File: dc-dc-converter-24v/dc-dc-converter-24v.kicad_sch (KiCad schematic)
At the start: 1 part, among them U1 LM5175PWPT

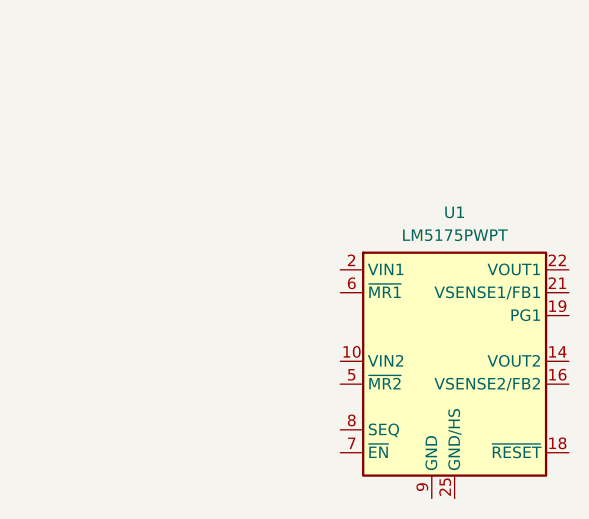
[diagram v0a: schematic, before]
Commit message: update symbol in DC-DC converter
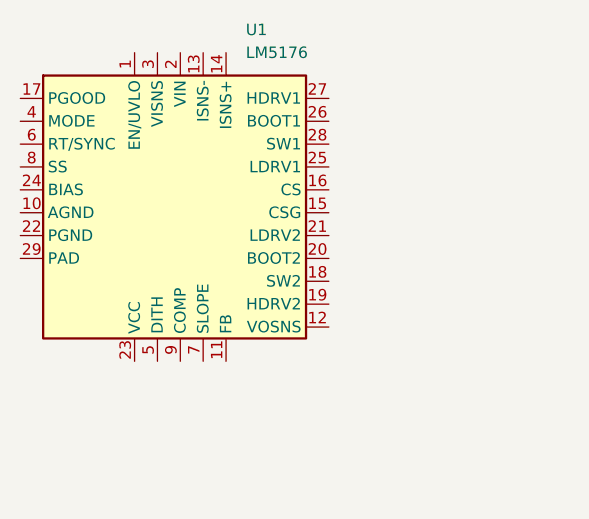
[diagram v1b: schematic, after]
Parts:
- removed U1: LM5175PWPT, benediktibk:LM5175PWPT, symbol benediktibk:LM5175PWPT
- added U1: LM5176, benediktibk:LM5176, symbol benediktibk:LM5176
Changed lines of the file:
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@@
 (kicad_sch (version 20230121) (generator eeschema)
   (paper "A4")
-  (symbol (lib_id "benediktibk:LM5175PWPT") (at 147.32 101.6 0) (unit 1)
+  (symbol (lib_id "benediktibk:LM5176") (at 111.76 82.55 0) (unit 1)
     (in_bom yes) (on_board yes) (dnp no) (fields_autoplaced)
-    (property "Reference" "U1" (at 147.32 85.09 0)
-      (effects (font (size 1.27 1.27)))
+    (property "Reference" "U1" (at 124.1141 64.77 0)
+      (effects (font (size 1.27 1.27)) (justify left))
     )
-    (property "Value" "LM5175PWPT" (at 147.32 87.63 0)
-      (effects (font (size 1.27 1.27)))
+    (property "Value" "LM5176" (at 124.1141 67.31 0)
+      (effects (font (size 1.27 1.27)) (justify left))
     )
-    (property "Footprint" "benediktibk:LM5175PWPT" (at 146.685 85.725 0)
+    (property "Footprint" "benediktibk:LM5176" (at 116.84 82.55 0)
       (effects (font (size 1.27 1.27) italic) hide)
     )
-    (property "Datasheet" "" (at 147.32 101.6 0)
+    (property "Datasheet" "" (at 111.76 82.55 0)
       (effects (font (size 1.27 1.27)) hide)
     )
-    (property "RS order number" "908-3877" (at 147.32 101.6 0)
+    (property "RS order number" "" (at 111.76 82.55 0)
       (effects (font (size 1.27 1.27)) hide)
     )
+    (pin "21")
+    (pin "7")
+    (pin "26")
+    (pin "24")
     (pin "22")
-    (pin "14")
-    (pin "2")
-    (pin "6")
-    (pin "3")
-    (pin "21")
-    (pin "17")
-    (pin "16")
-    (pin "7")
-    (pin "4")
-    (pin "9")
-    (pin "19")
-    (pin "5")
-    (pin "15")
-    (pin "23")
-    (pin "13")
-    (pin "24")
-    (pin "8")
-    (pin "1")
     (pin "11")
     (pin "10")
+    (pin "18")
+    (pin "25")
+    (pin "3")
+    (pin "6")
+    (pin "16")
+    (pin "28")
     (pin "20")
-    (pin "25")
+    (pin "2")
+    (pin "17")
+    (pin "19")
+    (pin "9")
+    (pin "1")
+    (pin "27")
+    (pin "23")
+    (pin "8")
+    (pin "5")
+    (pin "4")
+    (pin "13")
     (pin "12")
-    (pin "18")
+    (pin "14")
+    (pin "15")
+    (pin "29")
     (instances
       (project "dc-dc-converter-24v"

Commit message: work on DC DC converter
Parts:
- added C1: 470uF, symbol benediktibk:C_470uF_SMD_63V_20%
- added C2: C_240pF_SMD_0805_250V_10%, benediktibk:C_0805_2012Metric_Pad1.18x1.45mm_HandSolder, symbol benediktibk:C_240pF_SMD_0805_250V_10%
- added C3, C6: 47uF, benediktibk:C_1206_3216Metric_Pad1.33x1.80mm_HandSolder, symbol benediktibk:C_47uF_SMD_1206_25V_20%
- added C4, C5: 4.7uF, benediktibk:C_0805_2012Metric_Pad1.18x1.45mm_HandSolder, symbol benediktibk:C_4_7uF_SMD_0805_50V_10%
- added C7: 1uF, benediktibk:C_0603_1608Metric_Pad1.08x0.95mm_HandSolder, symbol benediktibk:C_1uF_SMD_0603_50V_10%
- added C8, C9: 100nF, benediktibk:C_0603_1608Metric_Pad1.08x0.95mm_HandSolder, symbol benediktibk:C_100nF_SMD_0603_50V
- added H1, H2, H3, H4: MountingHole_Pad_M6, benediktibk:MountingHole_6.4mm_M6_Pad_TopBottom, symbol benediktibk:MountingHole_Pad_M6
- added J1: 24V, benediktibk:Connector_M6, symbol benediktibk:Connector_M6
- added J2: 12V, benediktibk:Connector_M6, symbol benediktibk:Connector_M6
- added J3, J4: GND, benediktibk:Connector_M6, symbol benediktibk:Connector_M6
- added L1: L_2_5µH_30A, symbol benediktibk:L_2_5µH_30A
- added R1: 24kOhm, benediktibk:R_0603_1608Metric_Pad0.98x0.95mm_HandSolder, symbol benediktibk:R_24kOhm_SMD_0603_100mW_1%
- added R2: 4mOhm, benediktibk:R_2512_6332Metric_Pad1.40x3.35mm_HandSolder, symbol benediktibk:R_4mOhm_SMD_2512_2W_1%
- added R3: R_220kOhm_SMD_0603_100mW_1%, benediktibk:R_0603_1608Metric_Pad0.98x0.95mm_HandSolder, symbol benediktibk:R_220kOhm_SMD_0603_100mW_1%
- added R4: R_43kOhm_SMD_0603_100mW_1%, benediktibk:R_0603_1608Metric_Pad0.98x0.95mm_HandSolder, symbol benediktibk:R_43kOhm_SMD_0603_100mW_1%
- added R5: R_93_1kOhm_SMD_0603_100mW_1%, benediktibk:R_0603_1608Metric_Pad0.98x0.95mm_HandSolder, symbol benediktibk:R_93_1kOhm_SMD_0603_100mW_1%
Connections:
- net GND: now reaches U1.10 (AGND)
- net GND: now also U1.22 (PGND), U1.29 (PAD), C1.2, C2.2, C3.2, C4.2, C5.2, C6.2, C7.2, C8.2, C9.2, J3.1 (Pin_1), J4.1 (Pin_1), R1.2
- net Vout: now reaches U1.24 (BIAS)
- net Vout: now also C1.1, C3.1, C5.1, C8.1, J1.1 (Pin_1)
- net at U1.6 (RT/SYNC): now also R1.1
- net at U1.7 (SLOPE): now also C2.1
- net at U1.8 (SS): now also C9.1
- new net: C4.1, C6.1, C7.1, J2.1 (Pin_1)
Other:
- moved on the sheet: U1

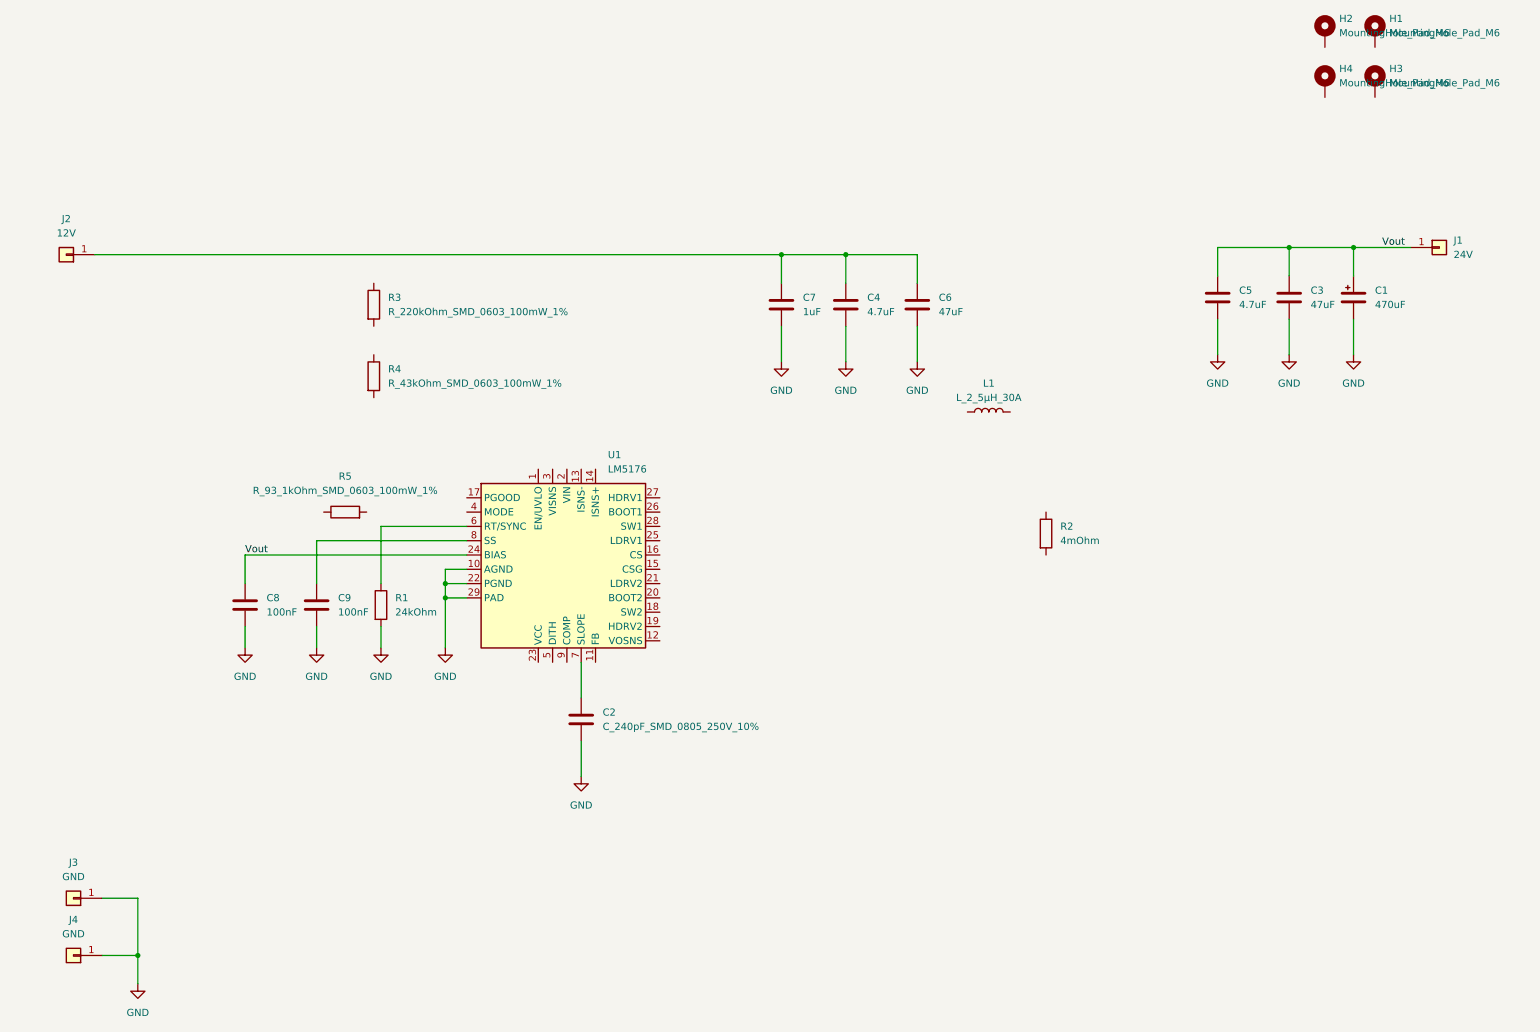
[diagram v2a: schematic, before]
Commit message: continue with design of DC-DC converter
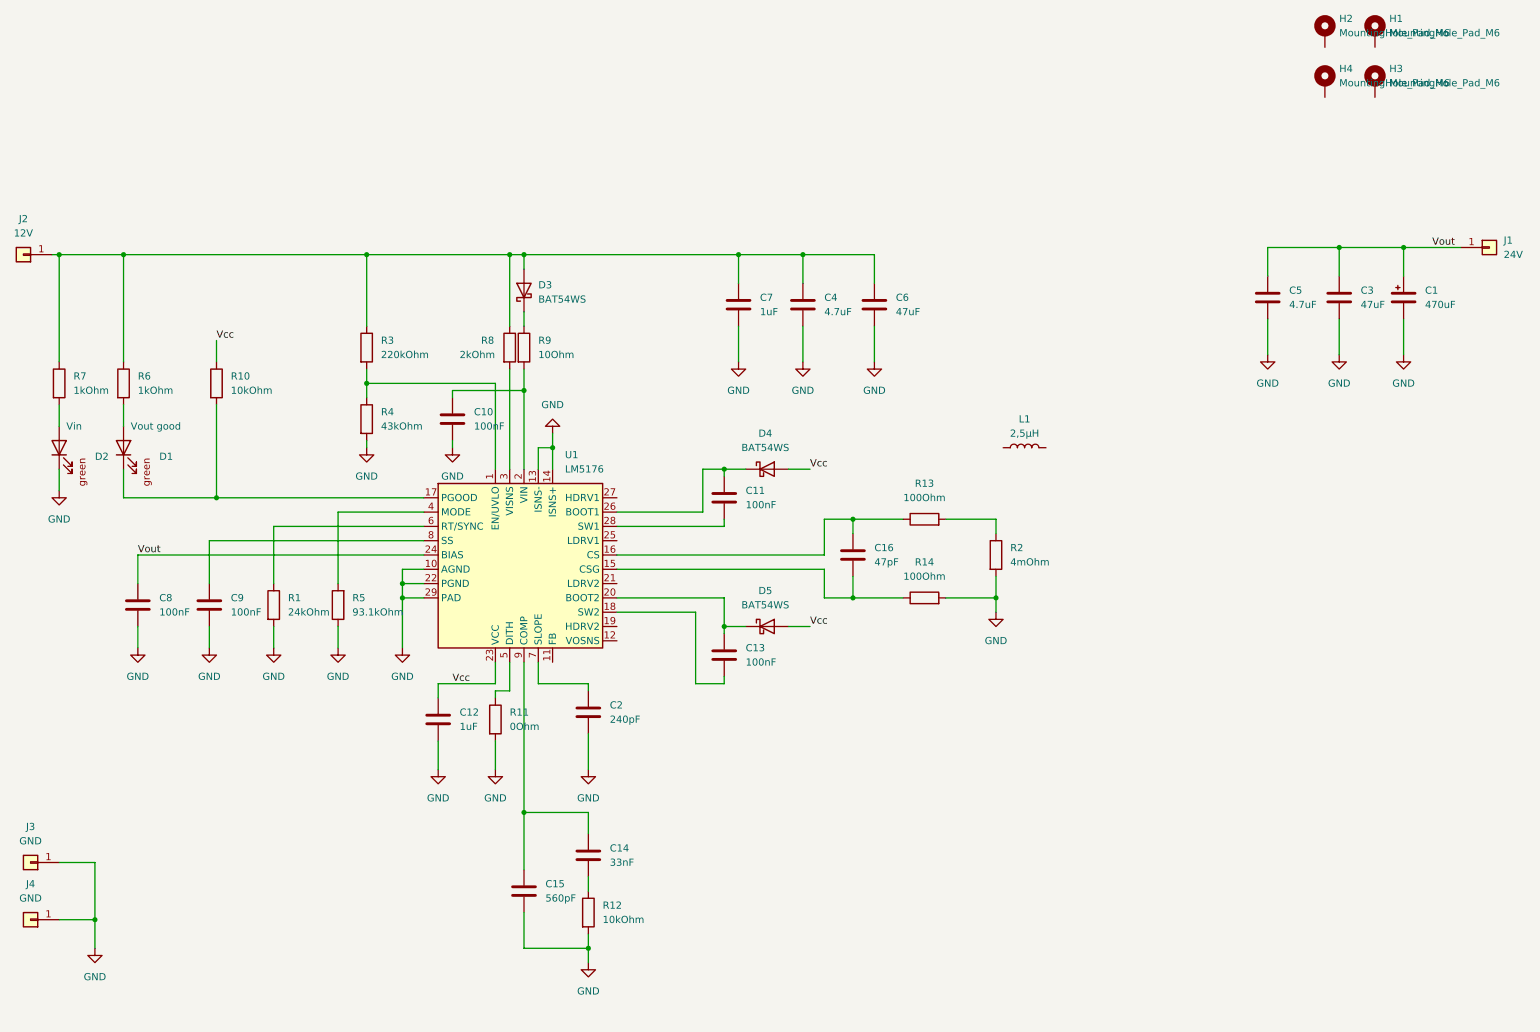
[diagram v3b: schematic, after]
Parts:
- added C10, C11, C13: 100nF, benediktibk:C_0603_1608Metric_Pad1.08x0.95mm_HandSolder, symbol benediktibk:C_100nF_SMD_0603_50V
- added C12: 1uF, benediktibk:C_0603_1608Metric_Pad1.08x0.95mm_HandSolder, symbol benediktibk:C_1uF_SMD_0603_50V_10%
- added C14: 33nF, benediktibk:C_0603_1608Metric_Pad1.08x0.95mm_HandSolder, symbol benediktibk:C_33nF_SMD_0603_50V_10%
- added C15: 560pF, benediktibk:C_0603_1608Metric_Pad1.08x0.95mm_HandSolder, symbol benediktibk:C_560pF_SMD_0603_50V_5%
- added C16: 47pF, benediktibk:C_0603_1608Metric_Pad1.08x0.95mm_HandSolder, symbol benediktibk:C_47pF_SMD_0603_100V_5%
- added D1: Vout good, benediktibk:D_0603_1608Metric_Pad1.05x0.95mm_HandSolder, symbol benediktibk:LED_green_0603
- added D2: Vin, benediktibk:D_0603_1608Metric_Pad1.05x0.95mm_HandSolder, symbol benediktibk:LED_green_0603
- added D3, D4, D5: BAT54WS, benediktibk:D_SOD-323, symbol benediktibk:BAT54WS
- added R10, R12: 10kOhm, benediktibk:R_0603_1608Metric_Pad0.98x0.95mm_HandSolder, symbol benediktibk:R_10kOhm_SMD_0603_100mW_1%
- added R11: 0Ohm, benediktibk:R_0603_1608Metric_Pad0.98x0.95mm_HandSolder, symbol benediktibk:R_0Ohm_SMD_0603_100mW_0%
- added R13, R14: 100Ohm, benediktibk:R_0603_1608Metric_Pad0.98x0.95mm_HandSolder, symbol benediktibk:R_100Ohm_SMD_0603_100mW_1%
- added R6, R7: 1kOhm, benediktibk:R_0603_1608Metric_Pad0.98x0.95mm_HandSolder, symbol benediktibk:R_1kOhm_SMD_0603_100mW_1%
- added R8: 2kOhm, benediktibk:R_0603_1608Metric_Pad0.98x0.95mm_HandSolder, symbol benediktibk:R_2kOhm_SMD_0603_100mW_1%
- added R9: 10Ohm, benediktibk:R_0603_1608Metric_Pad0.98x0.95mm_HandSolder, symbol benediktibk:R_10Ohm_SMD_0603_100mW_1%
- C2: value C_240pF_SMD_0805_250V_10% -> 240pF
- L1: value L_2_5µH_30A -> 2,5µH
- R3: value R_220kOhm_SMD_0603_100mW_1% -> 220kOhm
- R4: value R_43kOhm_SMD_0603_100mW_1% -> 43kOhm
- R5: value R_93_1kOhm_SMD_0603_100mW_1% -> 93.1kOhm; symbol benediktibk:R_93_1kOhm_SMD_0603_100mW_1% -> benediktibk:R_93_1kOhm_SMD_0603_100mW_0_1%
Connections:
- net GND: now also R2.2, R4.2, R5.1, U1.13 (ISNS-), U1.14 (ISNS+), C10.2, C12.2, C15.2, D2.1 (K), R11.2, R12.2, R14.2
- net at R2.1: now also R13.2
- net at U1.1 (EN/UVLO): now also R3.2, R4.1
- net at U1.15 (CSG): now also C16.2, R14.1
- net at U1.16 (CS): now also C16.1, R13.1
- net at U1.17 (PGOOD): now also D1.1 (K), R10.2
- net at U1.18 (SW2): now also C13.2
- net at U1.2 (VIN): now also C10.1, R9.2
- net at U1.20 (BOOT2): now also C13.1, D5.1 (K)
- net Vcc: now reaches U1.23 (VCC)
- net Vcc: now also C12.1, D4.2 (A), D5.2 (A), R10.1
- net at U1.26 (BOOT1): now also C11.1, D4.1 (K)
- net at U1.28 (SW1): now also C11.2
- net at U1.3 (VISNS): now also R8.2
- net at U1.4 (MODE): now also R5.2
- net at U1.5 (DITH): now also R11.1
- net at U1.9 (COMP): now also C14.1, C15.1
- net at C4.1, C6.1, C7.1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: now also R3.1, D3.2 (A), R6.1, R7.1, R8.1
- new net: C14.2, R12.1
- new net: D1.2 (A), R6.2
- new net: D2.2 (A), R7.2
- new net: D3.1 (K), R9.1
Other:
- moved on the sheet: C1, C2, C3, C4, C5, C6, C7, C8, C9, J1, J2, J3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

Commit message: select MOSFETs for DC-DC converter
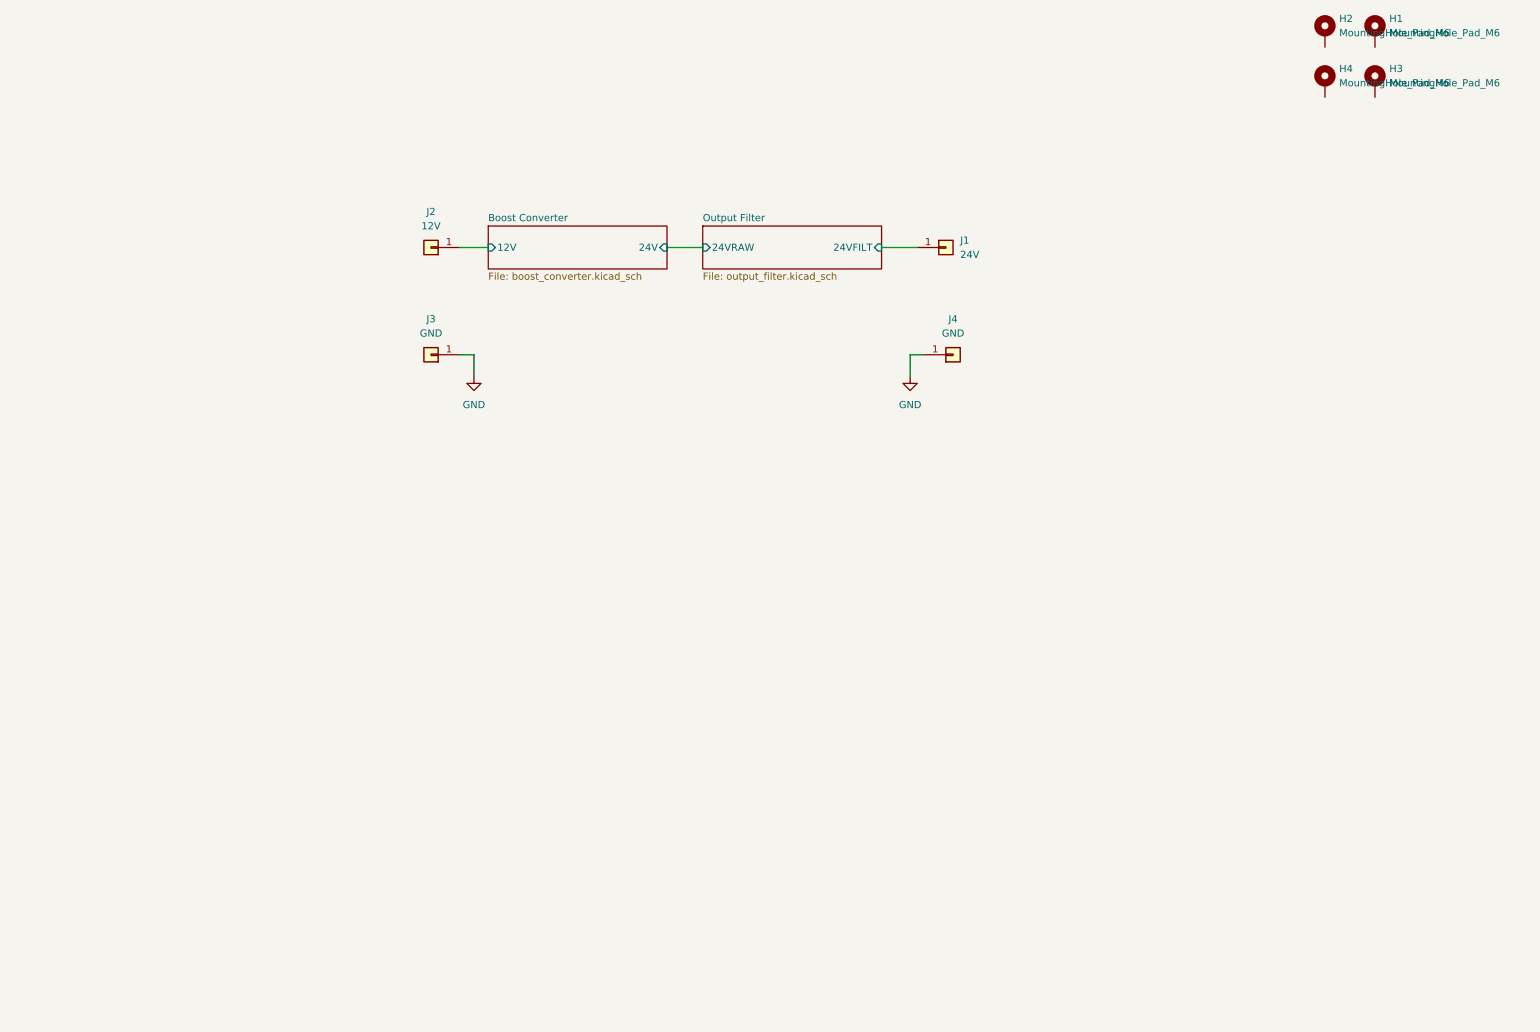
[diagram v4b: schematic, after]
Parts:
- removed C1: 470uF, symbol benediktibk:C_470uF_SMD_63V_20%
- removed C10, C11, C13, C8, C9: 100nF, benediktibk:C_0603_1608Metric_Pad1.08x0.95mm_HandSolder, symbol benediktibk:C_100nF_SMD_0603_50V
- removed C12, C7: 1uF, benediktibk:C_0603_1608Metric_Pad1.08x0.95mm_HandSolder, symbol benediktibk:C_1uF_SMD_0603_50V_10%
- removed C14: 33nF, benediktibk:C_0603_1608Metric_Pad1.08x0.95mm_HandSolder, symbol benediktibk:C_33nF_SMD_0603_50V_10%
- removed C15: 560pF, benediktibk:C_0603_1608Metric_Pad1.08x0.95mm_HandSolder, symbol benediktibk:C_560pF_SMD_0603_50V_5%
- removed C16: 47pF, benediktibk:C_0603_1608Metric_Pad1.08x0.95mm_HandSolder, symbol benediktibk:C_47pF_SMD_0603_100V_5%
- removed C2: 240pF, benediktibk:C_0805_2012Metric_Pad1.18x1.45mm_HandSolder, symbol benediktibk:C_240pF_SMD_0805_250V_10%
- removed C3, C6: 47uF, benediktibk:C_1206_3216Metric_Pad1.33x1.80mm_HandSolder, symbol benediktibk:C_47uF_SMD_1206_25V_20%
- removed C4, C5: 4.7uF, benediktibk:C_0805_2012Metric_Pad1.18x1.45mm_HandSolder, symbol benediktibk:C_4_7uF_SMD_0805_50V_10%
- removed D1: Vout good, benediktibk:D_0603_1608Metric_Pad1.05x0.95mm_HandSolder, symbol benediktibk:LED_green_0603
- removed D2: Vin, benediktibk:D_0603_1608Metric_Pad1.05x0.95mm_HandSolder, symbol benediktibk:LED_green_0603
- removed D3, D4, D5: BAT54WS, benediktibk:D_SOD-323, symbol benediktibk:BAT54WS
- removed L1: 2,5µH, symbol benediktibk:L_2_5µH_30A
- removed R1: 24kOhm, benediktibk:R_0603_1608Metric_Pad0.98x0.95mm_HandSolder, symbol benediktibk:R_24kOhm_SMD_0603_100mW_1%
- removed R10, R12: 10kOhm, benediktibk:R_0603_1608Metric_Pad0.98x0.95mm_HandSolder, symbol benediktibk:R_10kOhm_SMD_0603_100mW_1%
- removed R11: 0Ohm, benediktibk:R_0603_1608Metric_Pad0.98x0.95mm_HandSolder, symbol benediktibk:R_0Ohm_SMD_0603_100mW_0%
- removed R13, R14: 100Ohm, benediktibk:R_0603_1608Metric_Pad0.98x0.95mm_HandSolder, symbol benediktibk:R_100Ohm_SMD_0603_100mW_1%
- removed R2: 4mOhm, benediktibk:R_2512_6332Metric_Pad1.40x3.35mm_HandSolder, symbol benediktibk:R_4mOhm_SMD_2512_2W_1%
- removed R3: 220kOhm, benediktibk:R_0603_1608Metric_Pad0.98x0.95mm_HandSolder, symbol benediktibk:R_220kOhm_SMD_0603_100mW_1%
- removed R4: 43kOhm, benediktibk:R_0603_1608Metric_Pad0.98x0.95mm_HandSolder, symbol benediktibk:R_43kOhm_SMD_0603_100mW_1%
- removed R5: 93.1kOhm, benediktibk:R_0603_1608Metric_Pad0.98x0.95mm_HandSolder, symbol benediktibk:R_93_1kOhm_SMD_0603_100mW_0_1%
- removed R6, R7: 1kOhm, benediktibk:R_0603_1608Metric_Pad0.98x0.95mm_HandSolder, symbol benediktibk:R_1kOhm_SMD_0603_100mW_1%
- removed R8: 2kOhm, benediktibk:R_0603_1608Metric_Pad0.98x0.95mm_HandSolder, symbol benediktibk:R_2kOhm_SMD_0603_100mW_1%
- removed R9: 10Ohm, benediktibk:R_0603_1608Metric_Pad0.98x0.95mm_HandSolder, symbol benediktibk:R_10Ohm_SMD_0603_100mW_1%
- removed U1: LM5176, benediktibk:LM5176, symbol benediktibk:LM5176
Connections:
- net Boost Converter/12V: now reaches J2.1 (Pin_1)
- net Vout renamed Output Filter/24VFILT
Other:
- added sheet Boost Converter (boost_converter.kicad_sch)
- added sheet Output Filter (output_filter.kicad_sch)
- moved on the sheet: J1, J2, J3, J4
